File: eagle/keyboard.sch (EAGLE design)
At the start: 72 parts, among them IC1 STC12C5616AD, J4 RESERVED, Q1 12MHz

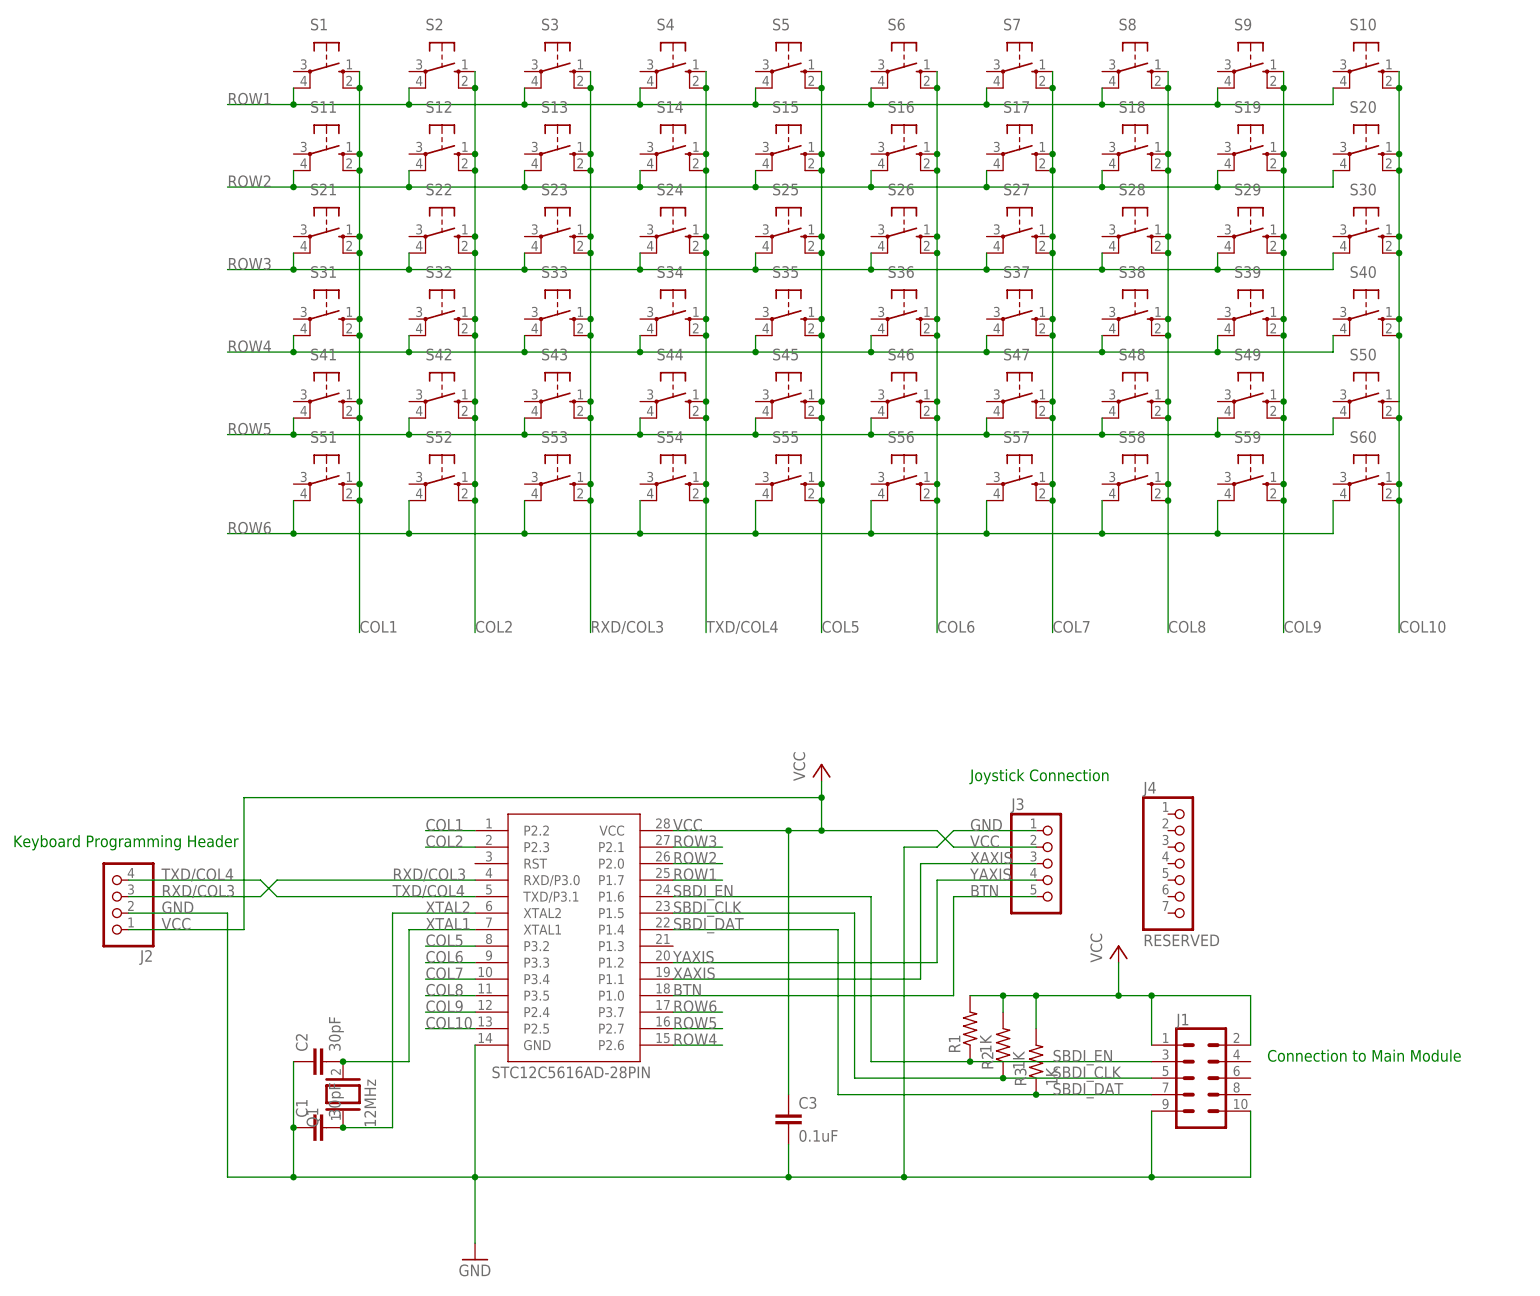
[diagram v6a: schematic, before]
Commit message: Add reset button to keyboard module
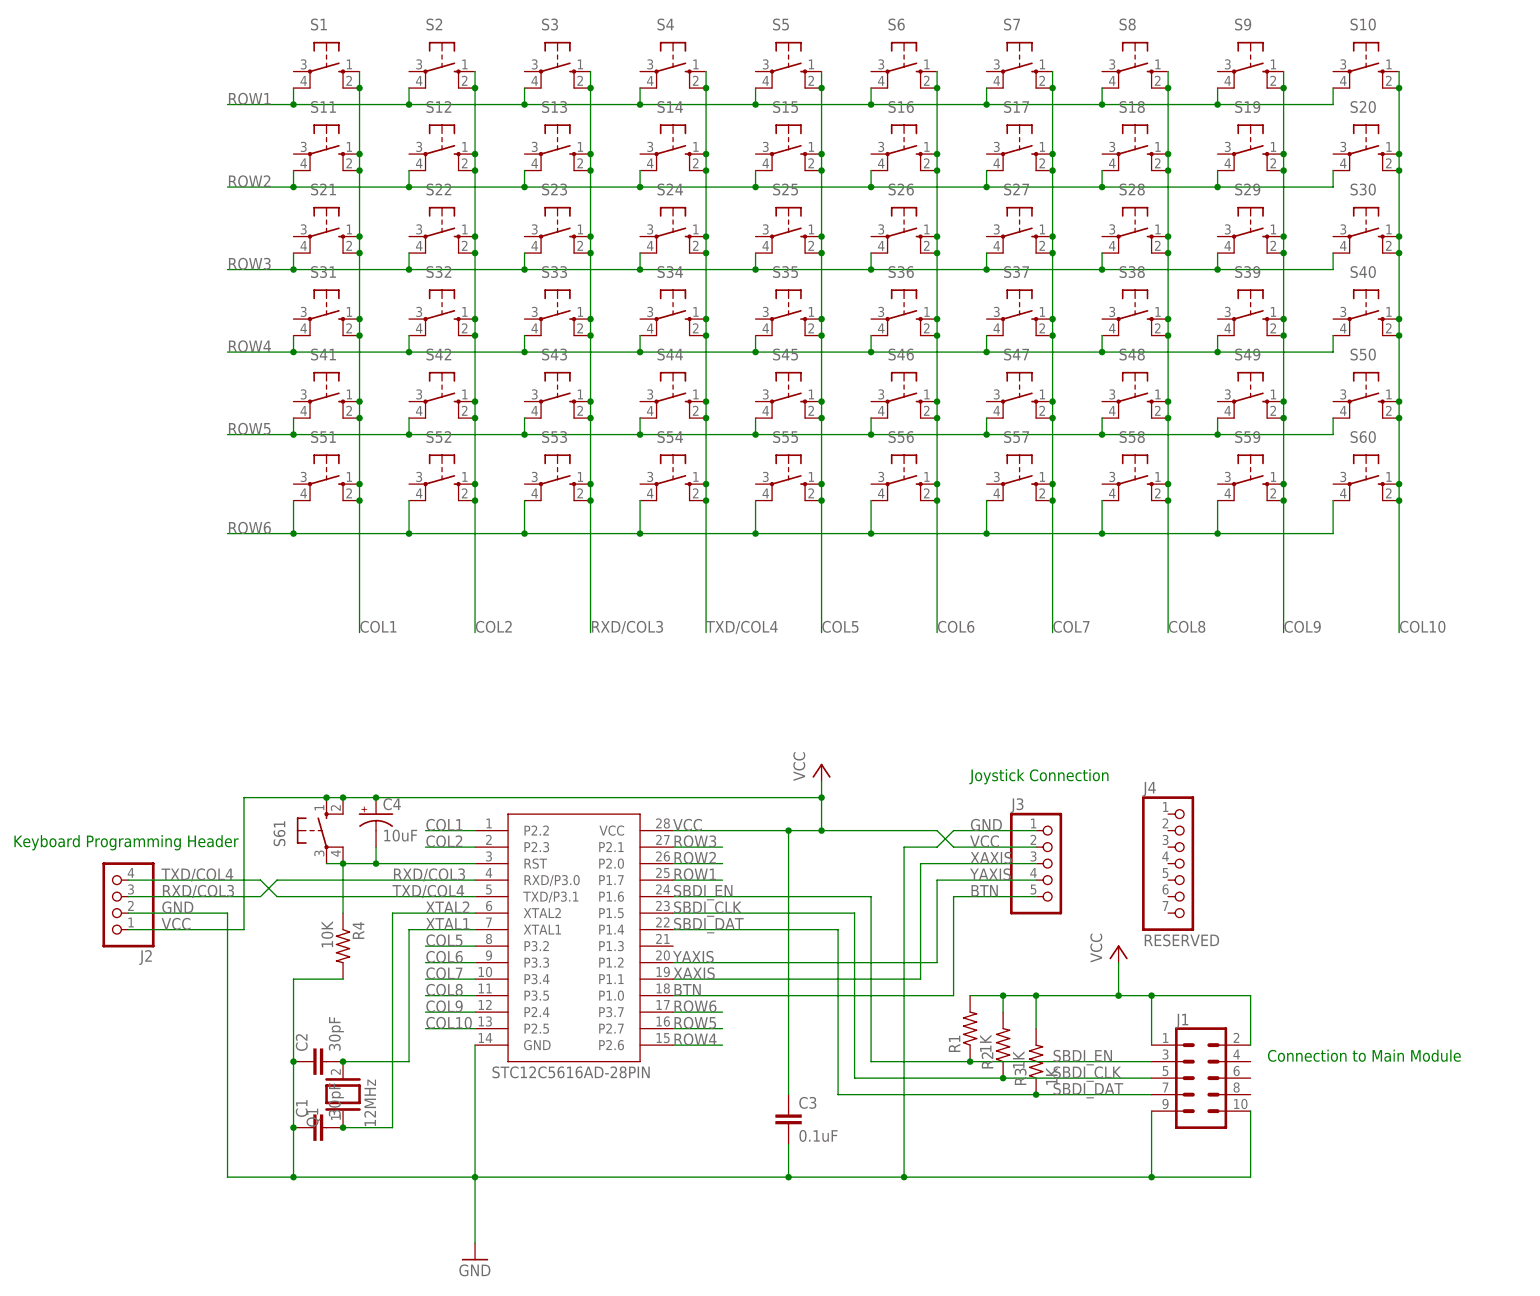
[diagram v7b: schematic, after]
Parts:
- added C4: 10uF, rcl:CPOL-USE1.8-4
- added R4: 10K, rcl:R-US_0204/7
- added S61: (no value), switch-omron:10-XX
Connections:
- new net N$2: C4.-, IC1.RST, R4.1, S61.P, S61.P1
- net GND: now also R4.2
- net VCC: now also C4.+, S61.S, S61.S1
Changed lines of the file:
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@@
 <part name="J2" library="pinhead" library_urn="urn:adsk.eagle:library:325" deviceset="PINHD-1X4" device="" package3d_urn="urn:adsk.eagle:package:22407/2"/>
 <part name="P+2" library="supply1" library_urn="urn:adsk.eagle:library:371" deviceset="VCC" device=""/>
-<part name="R1" library="rcl" library_urn="urn:adsk.eagle:library:334" deviceset="R-US_" device="0204/7" package3d_urn="urn:adsk.eagle:package:23498/1" value="1K"/>
-<part name="R2" library="rcl" library_urn="urn:adsk.eagle:library:334" deviceset="R-US_" device="0204/7" package3d_urn="urn:adsk.eagle:package:23498/1" value="1K"/>
-<part name="R3" library="rcl" library_urn="urn:adsk.eagle:library:334" deviceset="R-US_" device="0204/7" package3d_urn="urn:adsk.eagle:package:23498/1" value="1K"/>
+<part name="R1" library="rcl" library_urn="urn:adsk.eagle:library:334" deviceset="R-US_" device="0204/7" package3d_urn="urn:adsk.eagle:package:23498/2" value="1K"/>
+<part name="R2" library="rcl" library_urn="urn:adsk.eagle:library:334" deviceset="R-US_" device="0204/7" package3d_urn="urn:adsk.eagle:package:23498/2" value="1K"/>
+<part name="R3" library="rcl" library_urn="urn:adsk.eagle:library:334" deviceset="R-US_" device="0204/7" package3d_urn="urn:adsk.eagle:package:23498/2" value="1K"/>
 <part name="J1" library="SparkFun-Connectors" library_urn="urn:adsk.eagle:library:513" deviceset="CONN_05X2" device="SHD_LOCK" package3d_urn="urn:adsk.eagle:package:38007/1"/>
 <part name="C3" library="rcl" library_urn="urn:adsk.eagle:library:334" deviceset="C-EU" device="025-030X050" package3d_urn="urn:adsk.eagle:package:23631/1" value="0.1uF"/>
 <part name="J4" library="pinhead" library_urn="urn:adsk.eagle:library:325" deviceset="PINHD-1X7" device="" package3d_urn="urn:adsk.eagle:package:22477/2" value="RESERVED"/>
+<part name="C4" library="rcl" library_urn="urn:adsk.eagle:library:334" deviceset="CPOL-US" device="E1.8-4" package3d_urn="urn:adsk.eagle:package:23336/2" value="10uF"/>
+<part name="S61" library="switch-omron" library_urn="urn:adsk.eagle:library:377" deviceset="10-XX" device="" package3d_urn="urn:adsk.eagle:package:27496/1"/>
+<part name="R4" library="rcl" library_urn="urn:adsk.eagle:library:334" deviceset="R-US_" device="0204/7" package3d_urn="urn:adsk.eagle:package:23498/2" value="10K"/>
 </parts>
 <sheets>
@@
 <attribute name="NAME" x="196.85" y="84.455" size="1.778" layer="95"/>
 <attribute name="VALUE" x="196.85" y="60.96" size="1.778" layer="96"/>
+</instance>
+<instance part="C4" gate="G$1" x="78.74" y="81.28" smashed="yes">
+<attribute name="NAME" x="79.756" y="81.915" size="1.778" layer="95"/>
+<attribute name="VALUE" x="79.756" y="77.089" size="1.778" layer="96"/>
+</instance>
+<instance part="S61" gate="1" x="71.12" y="78.74" smashed="yes">
+<attribute name="NAME" x="64.77" y="76.2" size="1.778" layer="95" rot="R90"/>
+<attribute name="VALUE" x="67.31" y="81.915" size="1.778" layer="96" rot="R90"/>
+</instance>
+<instance part="R4" gate="G$1" x="73.66" y="60.96" smashed="yes" rot="R270">
+<attribute name="NAME" x="75.1586" y="64.77" size="1.778" layer="95" rot="R270"/>
+<attribute name="VALUE" x="70.358" y="64.77" size="1.778" layer="96" rot="R270"/>
 </instance>
 </instances>
@@
 <wire x1="142.24" y1="30.48" x2="142.24" y2="25.4" width="0.1524" layer="91"/>
 <junction x="142.24" y="25.4"/>
+<pinref part="R4" gate="G$1" pin="2"/>
+<wire x1="73.66" y1="55.88" x2="66.04" y2="55.88" width="0.1524" layer="91"/>
+<wire x1="66.04" y1="55.88" x2="66.04" y2="43.18" width="0.1524" layer="91"/>
+<junction x="66.04" y="43.18"/>
 </segment>
 </net>
@@
 <wire x1="236.22" y1="154.94" x2="236.22" y2="157.48" width="0.1524" layer="91"/>
 <junction x="236.22" y="157.48"/>
+<junction x="236.22" y="144.78"/>
 </segment>
 </net>
@@
 <wire x1="142.24" y1="78.74" x2="124.46" y2="78.74" width="0.1524" layer="91"/>
 <wire x1="147.32" y1="86.36" x2="147.32" y2="83.82" width="0.1524" layer="91"/>
-<pinref part="J2" gate="A" pin="1"/>
 <wire x1="147.32" y1="83.82" x2="147.32" y2="78.74" width="0.1524" layer="91"/>
-<wire x1="40.64" y1="63.5" x2="58.42" y2="63.5" width="0.1524" layer="91"/>
-<wire x1="58.42" y1="63.5" x2="58.42" y2="83.82" width="0.1524" layer="91"/>
-<wire x1="58.42" y1="83.82" x2="147.32" y2="83.82" width="0.1524" layer="91"/>
 <junction x="147.32" y="83.82"/>
-<label x="45.72" y="63.5" size="1.778" layer="95"/>
+<wire x1="78.74" y1="83.82" x2="147.32" y2="83.82" width="0.1524" layer="91"/>
 <wire x1="147.32" y1="78.74" x2="165.1" y2="78.74" width="0.1524" layer="91"/>
 <junction x="147.32" y="78.74"/>
@@
 <wire x1="142.24" y1="38.1" x2="142.24" y2="78.74" width="0.1524" layer="91"/>
 <junction x="142.24" y="78.74"/>
+<pinref part="C4" gate="G$1" pin="+"/>
+<junction x="78.74" y="83.82"/>
+<wire x1="73.66" y1="83.82" x2="78.74" y2="83.82" width="0.1524" layer="91"/>
+<pinref part="S61" gate="1" pin="S1"/>
+<wire x1="58.42" y1="83.82" x2="71.12" y2="83.82" width="0.1524" layer="91"/>
+<wire x1="58.42" y1="63.5" x2="58.42" y2="83.82" width="0.1524" layer="91"/>
+<pinref part="J2" gate="A" pin="1"/>
+<wire x1="40.64" y1="63.5" x2="58.42" y2="63.5" width="0.1524" layer="91"/>
+<label x="45.72" y="63.5" size="1.778" layer="95"/>
+<pinref part="S61" gate="1" pin="S"/>
+<wire x1="71.12" y1="83.82" x2="73.66" y2="83.82" width="0.1524" layer="91"/>
+<junction x="71.12" y="83.82"/>
+<junction x="73.66" y="83.82"/>
 </segment>
 <segment>
@@
 </segment>
 </net>
+<net name="N$2" class="0">
+<segment>
+<pinref part="S61" gate="1" pin="P"/>
+<pinref part="S61" gate="1" pin="P1"/>
+<wire x1="71.12" y1="73.66" x2="73.66" y2="73.66" width="0.1524" layer="91"/>
+<pinref part="C4" gate="G$1" pin="-"/>
+<wire x1="73.66" y1="73.66" x2="78.74" y2="73.66" width="0.1524" layer="91"/>
+<wire x1="78.74" y1="73.66" x2="78.74" y2="76.2" width="0.1524" layer="91"/>
+<junction x="73.66" y="73.66"/>
+<pinref part="IC1" gate="G$1" pin="RST"/>
+<wire x1="78.74" y1="73.66" x2="93.98" y2="73.66" width="0.1524" layer="91"/>
+<junction x="78.74" y="73.66"/>
+<pinref part="R4" gate="G$1" pin="1"/>
+<wire x1="73.66" y1="73.66" x2="73.66" y2="66.04" width="0.1524" layer="91"/>
+</segment>
+</net>
